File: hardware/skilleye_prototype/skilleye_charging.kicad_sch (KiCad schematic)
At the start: 14 parts, among them Q1 FS8205A, U1 TP4056-42-ESOP8, U2 DW01A

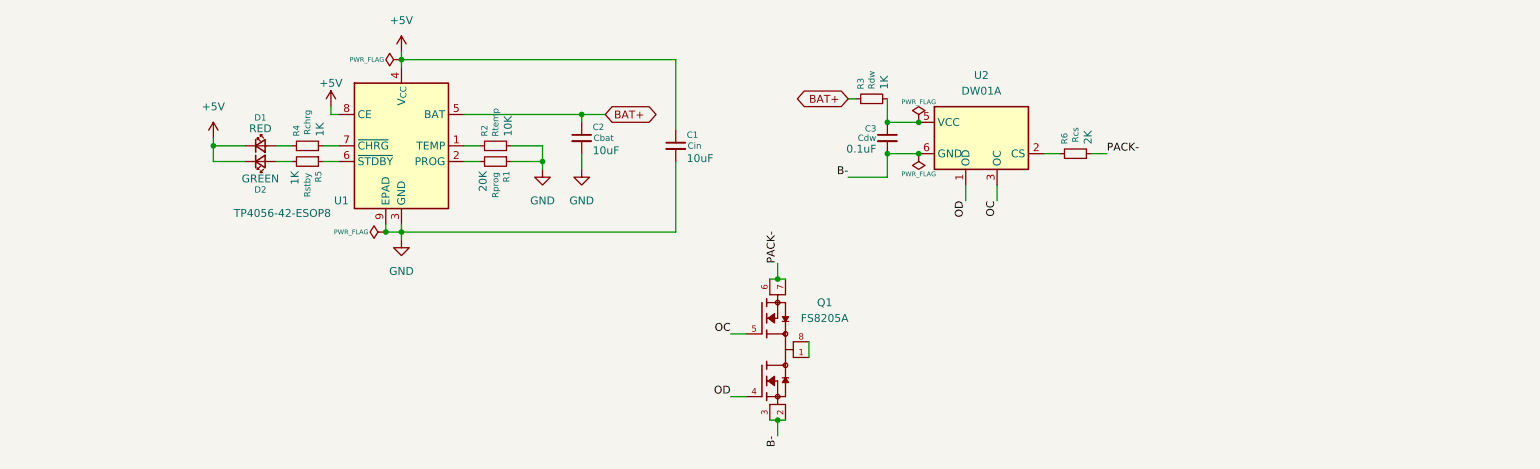
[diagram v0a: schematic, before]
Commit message: added regulator schematic + component libraries + datasheets
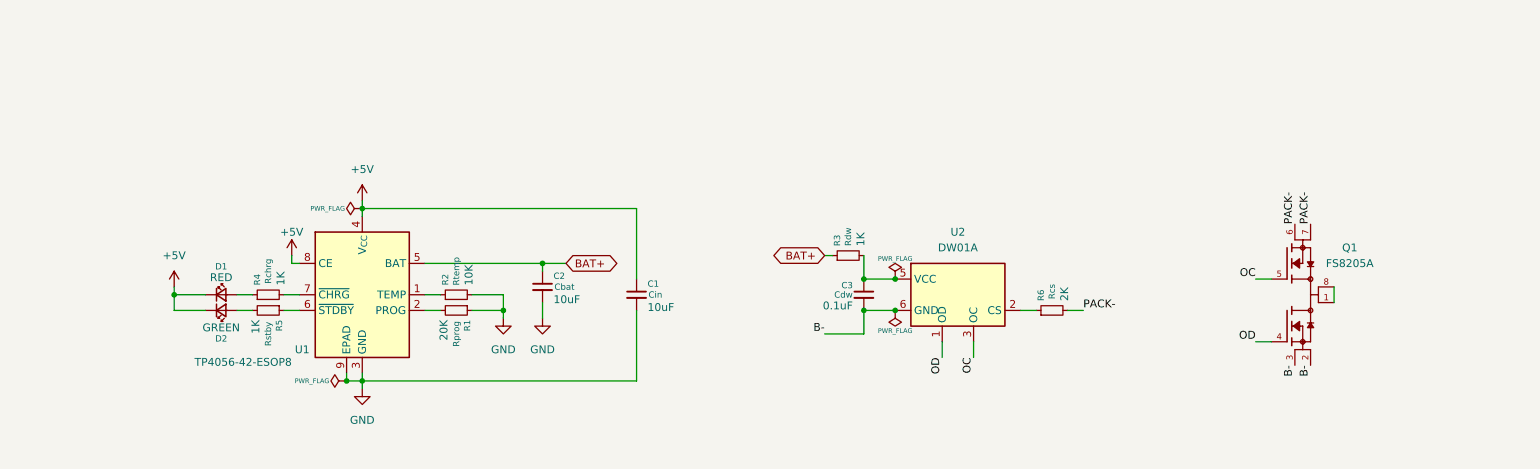
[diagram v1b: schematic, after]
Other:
- company: (none) -> National Taipei University of Technology - Dept. of EECS
- title: (none) -> Charging
- moved on the sheet: C1, C2, C3, D1, D2, Q1, R1, R2, R3, R4, R5, R6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

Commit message: added MCU schematic + datasheets
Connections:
- net GND: now also R6.2
- net PACK-: no longer R6.2
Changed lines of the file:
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@@
+	(wire
+		(pts
+			(xy 195.58 102.87) (xy 198.12 102.87)
+		)
+		(stroke
+			(width 0)
+			(type default)
+		)
+	)
 	(wire
 		(pts
@@
 	(wire
 		(pts
+			(xy 198.12 104.14) (xy 198.12 102.87)
+		)
+		(stroke
+			(width 0)
+			(type default)
+		)
+	)
+	(wire
+		(pts
 			(xy 91.44 102.87) (xy 93.98 102.87)
 		)
@@
 		(pts
 			(xy 81.28 114.3) (xy 125.73 114.3)
-		)
-		(stroke
-			(width 0)
-			(type default)
-		)
-	)
-	(wire
-		(pts
-			(xy 195.58 102.87) (xy 198.12 102.87)
 		)
 		(stroke
@@
 			)
 			(justify right bottom)
-		)
-	)
-	(label "PACK-"
-		(at 198.12 102.87 0)
-		(effects
-			(font
-				(size 1.27 1.27)
-			)
-			(justify left bottom)
 		)
 	)
@@
 		(dnp no)
 		(property "Reference" "R4"
-			(at 64.262 98.806 0)
+			(at 63.754 96.774 90)
 			(show_name no)
 			(do_not_autoplace no)
@@
 					(size 1.016 1.016)
 				)
-				(justify left)
+				(justify right)
 			)
 		)
 		(property "Value" "1K"
-			(at 68.072 98.806 0)
-			(show_name no)
-			(do_not_autoplace no)
-			(effects
-				(font
-					(size 1.27 1.27)
-				)
-				(justify left)
+			(at 63.754 98.552 90)
+			(show_name no)
+			(do_not_autoplace no)
+			(effects
+				(font
+					(size 1.27 1.27)
+				)
+				(justify right)
 			)
 		)
@@
 		)
 		(property "Description" "Rchrg"
-			(at 66.04 96.52 0)
+			(at 68.326 96.774 90)
 			(show_name no)
 			(do_not_autoplace no)
@@
 		(dnp no)
 		(property "Reference" "R3"
-			(at 158.242 92.456 0)
+			(at 158.115 90.297 90)
 			(show_name no)
 			(do_not_autoplace no)
@@
 					(size 1.016 1.016)
 				)
-				(justify left)
+				(justify right)
 			)
 		)
 		(property "Value" "1K"
-			(at 162.052 92.456 0)
-			(show_name no)
-			(do_not_autoplace no)
-			(effects
-				(font
-					(size 1.27 1.27)
-				)
-				(justify left)
+			(at 157.988 92.202 90)
+			(show_name no)
+			(do_not_autoplace no)
+			(effects
+				(font
+					(size 1.27 1.27)
+				)
+				(justify right)
 			)
 		)
@@
 		)
 		(property "Description" "Rdw"
-			(at 160.02 90.932 0)
+			(at 162.306 90.932 90)
 			(show_name no)
 			(do_not_autoplace no)
@@
 					(size 1.016 1.016)
 				)
+				(justify top)
 			)
 		)
@@
 		(dnp no)
 		(property "Reference" "R2"
-			(at 94.742 98.806 0)
+			(at 94.488 96.774 90)
 			(show_name no)
 			(do_not_autoplace no)
@@
 					(size 1.016 1.016)
 				)
-				(justify left)
+				(justify right)
 			)
 		)
 		(property "Value" "10K"
-			(at 98.552 98.806 0)
-			(show_name no)
-			(do_not_autoplace no)
-			(effects
-				(font
-					(size 1.27 1.27)
-				)
-				(justify left)
+			(at 94.488 98.552 90)
+			(show_name no)
+			(do_not_autoplace no)
+			(effects
+				(font
+					(size 1.27 1.27)
+				)
+				(justify right)
 			)
 		)
@@
 		)
 		(property "Description" "Rtemp"
-			(at 96.52 96.52 0)
+			(at 99.314 96.774 90)
 			(show_name no)
 			(do_not_autoplace no)
@@
 		(dnp no)
 		(property "Reference" "R5"
-			(at 67.818 104.394 0)
+			(at 64.008 104.902 90)
 			(show_name no)
 			(do_not_autoplace no)
@@
 		)
 		(property "Value" "1K"
-			(at 64.008 104.394 0)
+			(at 64.008 106.68 90)
 			(show_name no)
 			(do_not_autoplace no)
@@
 		)
 		(property "Description" "Rstby"
-			(at 66.04 106.68 0)
+			(at 68.58 104.902 90)
 			(show_name no)
 			(do_not_autoplace no)
@@
 		(dnp no)
 		(property "Reference" "R6"
-			(at 191.262 101.346 0)
+			(at 191.262 99.06 90)
 			(show_name no)
 			(do_not_autoplace no)
@@
 					(size 1.016 1.016)
 				)
-				(justify left)
+				(justify right)
 			)
 		)
 		(property "Value" "2K"
-			(at 195.072 101.346 0)
-			(show_name no)
-			(do_not_autoplace no)
-			(effects
-				(font
-					(size 1.27 1.27)
-				)
-				(justify left)
+			(at 191.135 100.965 90)
+			(show_name no)
+			(do_not_autoplace no)
+			(effects
+				(font
+					(size 1.27 1.27)
+				)
+				(justify right)
 			)
 		)
@@
 		)
 		(property "Description" "Rcs"
-			(at 193.04 99.822 0)
+			(at 195.199 99.695 90)
 			(show_name no)
 			(do_not_autoplace no)
@@
 					(size 1.016 1.016)
 				)
+				(justify top)
 			)
 		)
@@
 		(dnp no)
 		(property "Reference" "D2"
+			(at 58.42 105.664 0)
+			(show_name no)
+			(do_not_autoplace no)
+			(effects
+				(font
+					(size 1.016 1.016)
+				)
+			)
+		)
+		(property "Value" "GREEN"
 			(at 58.42 107.442 0)
-			(show_name no)
-			(do_not_autoplace no)
-			(effects
-				(font
-					(size 1.016 1.016)
-				)
-			)
-		)
-		(property "Value" "GREEN"
-			(at 58.42 105.664 0)
 			(show_name no)
 			(do_not_autoplace no)
@@
 	)
 	(symbol
+		(lib_id "power:GND")
+		(at 198.12 104.14 0)
+		(unit 1)
+		(body_style 1)
+		(exclude_from_sim no)
+		(in_bom yes)
+		(on_board yes)
+		(in_pos_files yes)
+		(dnp no)
+		(fields_autoplaced yes)
+		(property "Reference" "#PWR020"
+			(at 198.12 110.49 0)
+			(hide yes)
+			(show_name no)
+			(do_not_autoplace no)
+			(effects
+				(font
+					(size 1.27 1.27)
+				)
+			)
+		)
+		(property "Value" "GND"
+			(at 198.12 109.22 0)
+			(show_name no)
+			(do_not_autoplace no)
+			(effects
+				(font
+					(size 1.27 1.27)
+				)
+			)
+		)
+		(property "Footprint" ""
+			(at 198.12 104.14 0)
+			(hide yes)
+			(show_name no)
+			(do_not_autoplace no)
+			(effects
+				(font
+					(size 1.27 1.27)
+				)
+			)
+		)
+		(property "Datasheet" ""
+			(at 198.12 104.14 0)
+			(hide yes)
+			(show_name no)
+			(do_not_autoplace no)
+			(effects
+				(font
+					(size 1.27 1.27)
+				)
+			)
+		)
+		(property "Description" "Power symbol creates a global label with name \"GND\" , ground"
+			(at 198.12 104.14 0)
+			(hide yes)
+			(show_name no)
+			(do_not_autoplace no)
+			(effects
+				(font
+					(size 1.27 1.27)
+				)
+			)
+		)
+		(pin "1"
+		)
+		(instances
+			(project "skilleye_prototype"
+				(path "/e922ced9-cce7-4ffa-8992-2bb79546169b/772fd356-96ac-42b2-8558-9fa39f1e8a4f"
+					(reference "#PWR020")
+					(unit 1)
+				)
+			)
+		)
+	)
+	(symbol
 		(lib_id "Device:C_Small")
 		(at 110.49 99.06 0)
@@
 		(dnp no)
 		(property "Reference" "R1"
-			(at 98.298 104.394 0)
+			(at 94.488 104.902 90)
 			(show_name no)
 			(do_not_autoplace no)
@@
 		)
 		(property "Value" "20K"
-			(at 94.488 104.394 0)
+			(at 94.488 106.68 90)
 			(show_name no)
 			(do_not_autoplace no)
@@
 		)
 		(property "Description" "Rprog"
-			(at 96.52 106.68 0)
-			(show_name no)
-			(do_not_autoplace no)
+			(at 99.06 104.902 90)
+			(show_name no)
+			(do_not_autoplace no)

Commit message: complete prototype rev1.0 schematics
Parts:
- added J1: Conn_01x02_Pin, symbol Connector:Conn_01x02_Pin
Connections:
- net PACK- is gone; now on net GND: Q1.6, Q1.7
- net B-: now also J1.2 (Pin_2)
- net BAT+: now also J1.1 (Pin_1)
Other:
- moved on the sheet: C1, C2, C3, D1, D2, Q1, R1, R2, R3, R4, R5, R6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

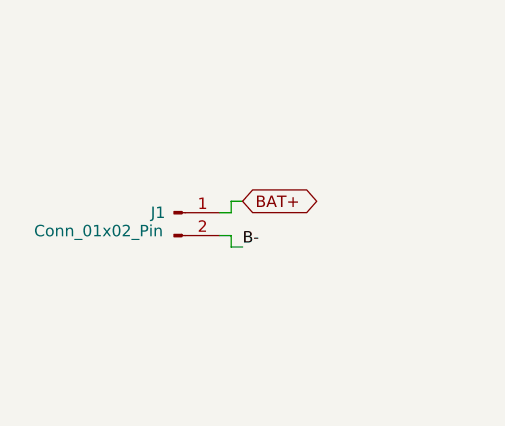
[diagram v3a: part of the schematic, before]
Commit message: prototype schematic rev1.1 - add VBUS sense divider
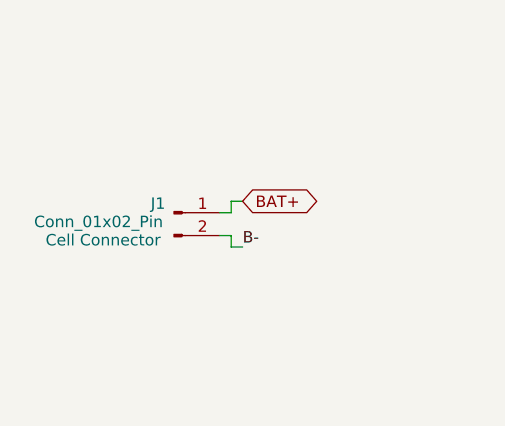
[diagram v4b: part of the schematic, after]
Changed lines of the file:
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@@
 	(title_block
 		(title "Charging")
-		(date "2026-07-21")
-		(rev "1.0")
+		(date "2026-07-23")
+		(rev "1.1")
 		(company "National Taipei University of Technology - Dept. of EECS")
 		(comment 1 "SkillEye")
@@
 		(dnp no)
 		(property "Reference" "J1"
-			(at 40.132 97.79 0)
+			(at 40.132 96.774 0)
 			(show_name no)
 			(do_not_autoplace no)
@@
 		)
 		(property "Value" "Conn_01x02_Pin"
-			(at 33.528 99.822 0)
+			(at 33.528 98.806 0)
 			(show_name no)
 			(do_not_autoplace no)
@@
 			)
 		)
-		(property "Description" "Generic connector, single row, 01x02, script generated"
-			(at 41.91 97.79 0)
-			(hide yes)
-			(show_name no)
-			(do_not_autoplace no)
+		(property "Description" "Cell Connector"
+			(at 34.036 100.838 0)
+			(show_name no)
+			(do_not_autoplace no)
